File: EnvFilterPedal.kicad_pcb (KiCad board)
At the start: 4 copper layers, 80 x 52 mm, 114 parts, among them J101 ScopeGroundLoop, J102 IO, Q101 BC857, Q102 BC857, Q103 BC847, U101 TL074, U102 TL074, U103 TL074, U104 LM13700, U105 AZ34063U

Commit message: component tweaks after playing thru it for a day
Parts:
- C110: value 10n -> 33n
- R109: value 6k8 -> 5k6
- R111: value 6k8 -> 12k
- R119: value 1k8 -> 2k2
- R136: value 1k8 -> 6k8
- R154: value 4k7 -> 6k8
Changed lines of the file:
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@@
 			)
 		)
-		(property "Value" "10n"
+		(property "Value" "33n"
 			(at 0 -1.679999 90)
 			(layer "B.Fab")
@@
 			)
 		)
-		(property "Value" "1k8"
+		(property "Value" "6k8"
 			(at 0 -1.65 90)
 			(layer "B.Fab")
@@
 			)
 		)
-		(property "Value" "6k8"
+		(property "Value" "12k"
 			(at 0 -1.65 90)
 			(layer "B.Fab")
@@
 			)
 		)
-		(property "Value" "6k8"
+		(property "Value" "5k6"
 			(at 0 -1.65 0)
 			(layer "B.Fab")
@@
 			)
 		)
-		(property "Value" "4k7"
+		(property "Value" "6k8"
 			(at 0 -1.65 0)
 			(layer "B.Fab")
@@
 			)
 		)
-		(property "Value" "1k8"
+		(property "Value" "2k2"
 			(at 0 -1.65 90)
 			(layer "B.Fab")

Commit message: minor value tweaks
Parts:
- R109: value 5k6 -> 5k1
- R111: value 12k -> 10k
- R154: value 6k8 -> 12k
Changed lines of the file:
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@@
 			)
 		)
-		(property "Value" "12k"
+		(property "Value" "10k"
 			(at 0 -1.65 90)
 			(layer "B.Fab")
@@
 			)
 		)
-		(property "Value" "5k6"
+		(property "Value" "5k1"
 			(at 0 -1.65 0)
 			(layer "B.Fab")
@@
 			)
 		)
-		(property "Value" "6k8"
+		(property "Value" "12k"
 			(at 0 -1.65 0)
 			(layer "B.Fab")

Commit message: added SMPS input filtering
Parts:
- added C1: 220u, Capacitor_THT:CP_Radial_D5.0mm_P2.00mm, B.Cu at (69.5, 88.2)
- added FB1: 90R, Inductor_SMD:L_0805_2012Metric, F.Cu at (68.9, 85.5)
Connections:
- C127 pad 1: +9V -> Net-(U105-VCC)
- R148 pad 1: +9V -> Net-(U105-VCC)
- U105 pad 6: +9V -> Net-(U105-VCC)
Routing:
- net Net-(U105-VCC): track 0.00 -> 22.2 mm
- net +9V: track 199.0 -> 182.5 mm
- net GND: vias 106 -> 103

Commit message: rev3 sent to fab
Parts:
- moved FB1 1.10 mm to (70.0, 85.5)
- turned TP101 to 180 degrees
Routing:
- net Net-(R140-Pad2): track 73.1 -> 71.5 mm
- net +9V: track 182.5 -> 183.6 mm
- net GND: vias 103 -> 102
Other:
- board text added: "Rev. 3- Feb 2025 Hayden Setlik"
- board text removed: "Rev. 2- Jan 2025 Hayden Setlik"
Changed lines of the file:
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@@
 	(footprint "Inductor_SMD:L_0805_2012Metric"
 		(layer "F.Cu")
-		(at 68.9 85.5)
+		(at 70 85.5)
 		(descr "Inductor SMD 0805 (2012 Metric), square (rectangular) end terminal, IPC_7351 nominal, (Body size source: IPC-SM-782 page 80, https://www.pcb-3d.com/wordpress/wp-content/uploads/ipc-sm-782a_amendment_1_and_2.pdf), generated with kicad-footprint-generator")
 		(tags "inductor")
@@
 	(footprint "TestPoint:TestPoint_THTPad_D2.0mm_Drill1.0mm_VAL"
 		(layer "B.Cu")
-		(at 39.6 65.275)
+		(at 39.6 65.275 180)
 		(descr "THT pad as test Point, diameter 1.5mm, hole diameter 0.7mm")
 		(tags "test point THT pad")
 		(property "Reference" "TP101"
-			(at 0 1.648 0)
+			(at 0 1.648 360)
 			(layer "B.SilkS")
 			(hide yes)
@@
 		)
 		(property "Value" "In"
-			(at 0 -2.000001 0)
+			(at 0 -2.000001 360)
 			(layer "B.SilkS")
 			(effects
@@
 		)
 		(property "Footprint" "TestPoint:TestPoint_THTPad_D2.0mm_Drill1.0mm_VAL"
-			(at 0 0 180)
+			(at 0 0 0)
 			(unlocked yes)
 			(layer "B.Fab")
@@
 		)
 		(property "Datasheet" ""
-			(at 0 0 180)
+			(at 0 0 0)
 			(unlocked yes)
 			(layer "B.Fab")
@@
 		)
 		(property "Description" "test point"
-			(at 0 0 180)
+			(at 0 0 0)
 			(unlocked yes)
 			(layer "B.Fab")
@@
 		)
 		(fp_text user "${VALUE}"
-			(at 0.01 -2.600001 180)
+			(at 0.01 -2.600001 0)
 			(unlocked yes)
 			(layer "F.SilkS")
@@
 		)
 		(fp_text user "${REFERENCE}"
-			(at 0 1.65 0)
+			(at 0 1.65 360)
 			(layer "B.Fab")
 			(effects
@@
 		)
 		(pad "1" thru_hole circle
-			(at 0 0)
+			(at 0 0 180)
 			(size 2 2)
 			(drill 1)
@@
 		)
 	)
-	(gr_text "Rev. 2- Jan 2025\nHayden Setlik"
+	(gr_text "Rev. 3- Feb 2025\nHayden Setlik"
 		(at 82.75 52.25 0)
 		(layer "B.SilkS")
@@
 	)
 	(via
-		(at 71.05 85.75)
-		(size 0.8)
-		(drill 0.4)
-		(layers "F.Cu" "B.Cu")
-		(free yes)
-		(net 1)
-	)
-	(via
 		(at 78.65 80.05)
 		(size 0.6)
@@
 	)
 	(segment
-		(start 44.95 62.45)
-		(end 44.95 60.65)
+		(start 67.8 85.5)
+		(end 65 88.3)
 		(width 0.35)
 		(layer "F.Cu")
@@
 	)
 	(segment
-		(start 8.1 63.45)
-		(end 14.025 57.525)
+		(start 65 88.3)
+		(end 58.85 88.3)
 		(width 0.35)
 		(layer "F.Cu")
@@
 	)
 	(segment
-		(start 50.25 76.1)
-		(end 50.25 77.5)
+		(start 44.95 62.45)
+		(end 44.95 60.65)
 		(width 0.35)
 		(layer "F.Cu")
@@
 	)
 	(segment
-		(start 67.8 85.5)
-		(end 65 88.3)
+		(start 8.1 63.45)
+		(end 14.025 57.525)
 		(width 0.35)
 		(layer "F.Cu")
@@
 	)
 	(segment
-		(start 67.8375 85.5)
-		(end 67.8 85.5)
+		(start 50.25 76.1)
+		(end 50.25 77.5)
 		(width 0.35)
 		(layer "F.Cu")
@@
 	)
 	(segment
+		(start 55.375 84.825)
+		(end 50.25 84.825)
+		(width 0.35)
+		(layer "F.Cu")
+		(net 3)
+	)
+	(segment
 		(start 8.15 78.75)
 		(end 8.1 78.7)
@@
 	)
 	(segment
-		(start 55.375 84.825)
-		(end 50.25 84.825)
-		(width 0.35)
-		(layer "F.Cu")
-		(net 3)
-	)
-	(segment
 		(start 24.7 46.85)
 		(end 30.715 46.85)
@@
 	)
 	(segment
-		(start 58.85 88.3)
-		(end 55.375 84.825)
+		(start 44.95 62.45)
+		(end 52 62.45)
 		(width 0.35)
 		(layer "F.Cu")
@@
 	)
 	(segment
-		(start 44.95 62.45)
-		(end 52 62.45)
+		(start 52 62.45)
+		(end 55.15 65.6)
 		(width 0.35)
 		(layer "F.Cu")
@@
 	)
 	(segment
-		(start 52 62.45)
-		(end 55.15 65.6)
+		(start 58.85 88.3)
+		(end 55.375 84.825)
 		(width 0.35)
 		(layer "F.Cu")
@@
 	)
 	(segment
-		(start 14.025 57.525)
-		(end 24.7 46.85)
+		(start 68.9375 85.5)
+		(end 67.8 85.5)
 		(width 0.35)
 		(layer "F.Cu")
@@
 	)
 	(segment
-		(start 55.15 65.6)
-		(end 55.15 71.2)
+		(start 14.025 57.525)
+		(end 24.7 46.85)
 		(width 0.35)
 		(layer "F.Cu")
@@
 	)
 	(segment
-		(start 65 88.3)
-		(end 58.85 88.3)
+		(start 55.15 65.6)
+		(end 55.15 71.2)
 		(width 0.35)
 		(layer "F.Cu")
@@
 	(segment
 		(start 64.775 77.700001)
-		(end 57.544999 77.700001)
+		(end 64.525001 77.95)
 		(width 0.18)
 		(layer "B.Cu")
@@
 	)
 	(segment
+		(start 64.525001 77.95)
+		(end 57.295 77.95)
+		(width 0.18)
+		(layer "B.Cu")
+		(net 9)
+	)
+	(segment
 		(start 57.1925 62.3425)
 		(end 52.275 62.3425)
@@
 	)
 	(segment
-		(start 57.544999 77.700001)
+		(start 57.295 77.95)
 		(end 57.275 77.97)
 		(width 0.18)
@@
 	)
 	(segment
-		(start 52.6 85.6)
-		(end 51.15 87.05)
+		(start 67 93)
+		(end 67 90.95)
 		(width 0.18)
 		(layer "B.Cu")
@@
 	)
 	(segment
-		(start 67 93)
-		(end 67 88.3)
+		(start 43.05 84.95)
+		(end 40.25 87.75)
 		(width 0.18)
 		(layer "B.Cu")
@@
 	)
 	(segment
-		(start 13.08 80.7825)
-		(end 11.775 82.0875)
+		(start 61.65 85.6)
+		(end 52.6 85.6)
 		(width 0.18)
 		(layer "B.Cu")
@@
 	)
 	(segment
-		(start 48.4 87.05)
-		(end 46.3 84.95)
+		(start 13.08 80.7825)
+		(end 11.775 82.0875)
 		(width 0.18)
 		(layer "B.Cu")
@@
 	)
 	(segment
-		(start 46.3 84.95)
-		(end 43.05 84.95)
+		(start 52.6 85.6)
+		(end 51.15 87.05)
 		(width 0.18)
 		(layer "B.Cu")
@@
 	)
 	(segment
-		(start 51.15 87.05)
-		(end 48.4 87.05)
+		(start 14.25 80.7825)
+		(end 13.08 80.7825)
 		(width 0.18)
 		(layer "B.Cu")
@@
 	)
 	(segment
-		(start 14.25 80.7825)
-		(end 13.08 80.7825)
+		(start 46.3 84.95)
+		(end 43.05 84.95)
 		(width 0.18)
 		(layer "B.Cu")
@@
 	)
 	(segment
-		(start 64.3 85.6)
-		(end 52.6 85.6)
+		(start 51.15 87.05)
+		(end 48.4 87.05)
 		(width 0.18)
 		(layer "B.Cu")
@@
 	)
 	(segment
-		(start 43.05 84.95)
-		(end 40.25 87.75)
+		(start 48.4 87.05)
+		(end 46.3 84.95)
 		(width 0.18)
 		(layer "B.Cu")
@@
 	)
 	(segment
-		(start 67 88.3)
-		(end 64.3 85.6)
+		(start 67 90.95)
+		(end 61.65 85.6)
 		(width 0.18)
 		(layer "B.Cu")
@@
 	)
 	(segment
+		(start 71.0625 86.4875)
+		(end 71.0625 85.5)
+		(width 0.35)
+		(layer "F.Cu")
+		(net 71)
+	)
+	(segment
 		(start 71.9 90.75)
 		(end 71.9 89.35)
@@
 	)
 	(segment
-		(start 69.55 88.25)
-		(end 69.55 85.9125)
-		(width 0.35)
-		(layer "F.Cu")
-		(net 71)
-	)
-	(segment
 		(start 78.155 92.795001)
 		(end 78.125 92.825001)
@@
 	)
 	(segment
+		(start 69.55 88)
+		(end 71.0625 86.4875)
+		(width 0.35)
+		(layer "F.Cu")
+		(net 71)
+	)
+	(segment
 		(start 71.9 89.35)
 		(end 70.8 88.25)
@@
 	)
 	(segment
-		(start 69.55 85.9125)
-		(end 69.9625 85.5)
+		(start 78.174999 92.875)
+		(end 78.125 92.825001)
 		(width 0.35)
 		(layer "F.Cu")
@@
 	)
 	(segment
-		(start 78.174999 92.875)
-		(end 78.125 92.825001)
+		(start 69.55 88.25)
+		(end 69.55 88)
 		(width 0.35)
 		(layer "F.Cu")

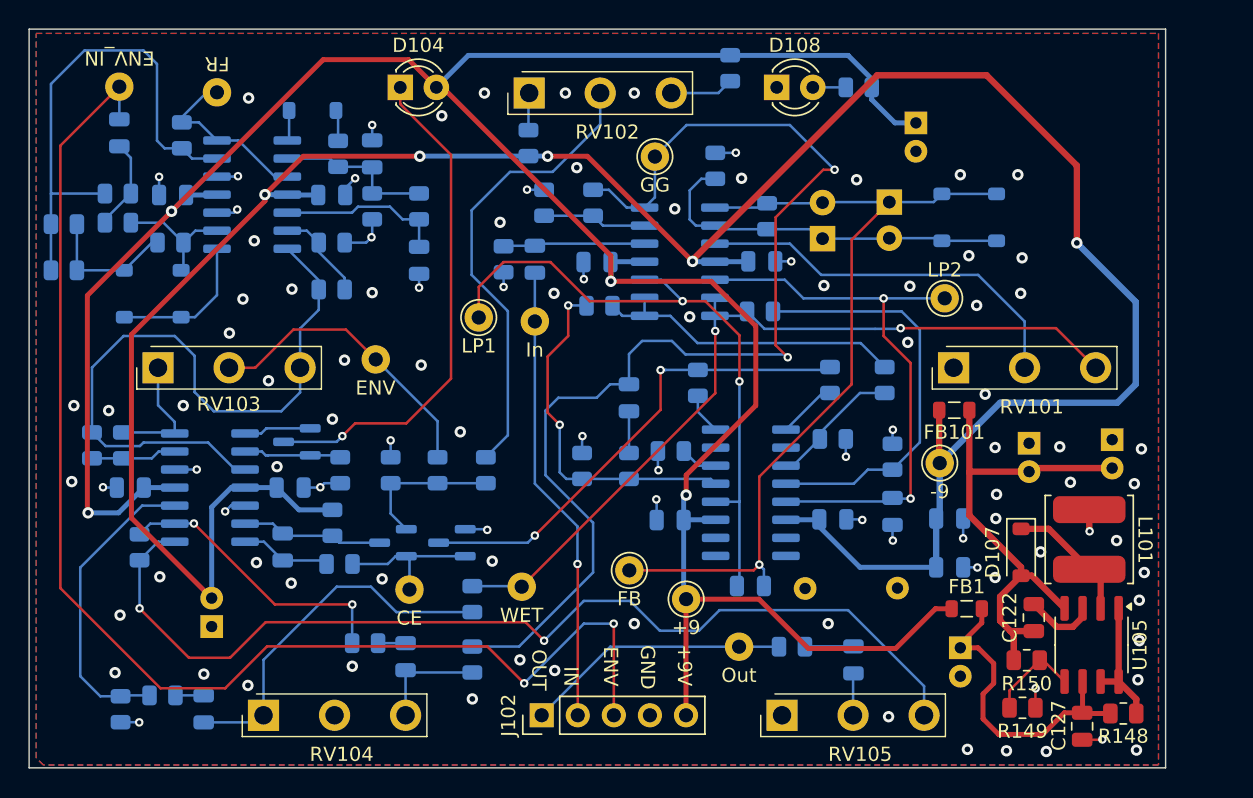
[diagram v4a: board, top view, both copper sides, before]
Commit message: laid out new inductor, some trace cleanup
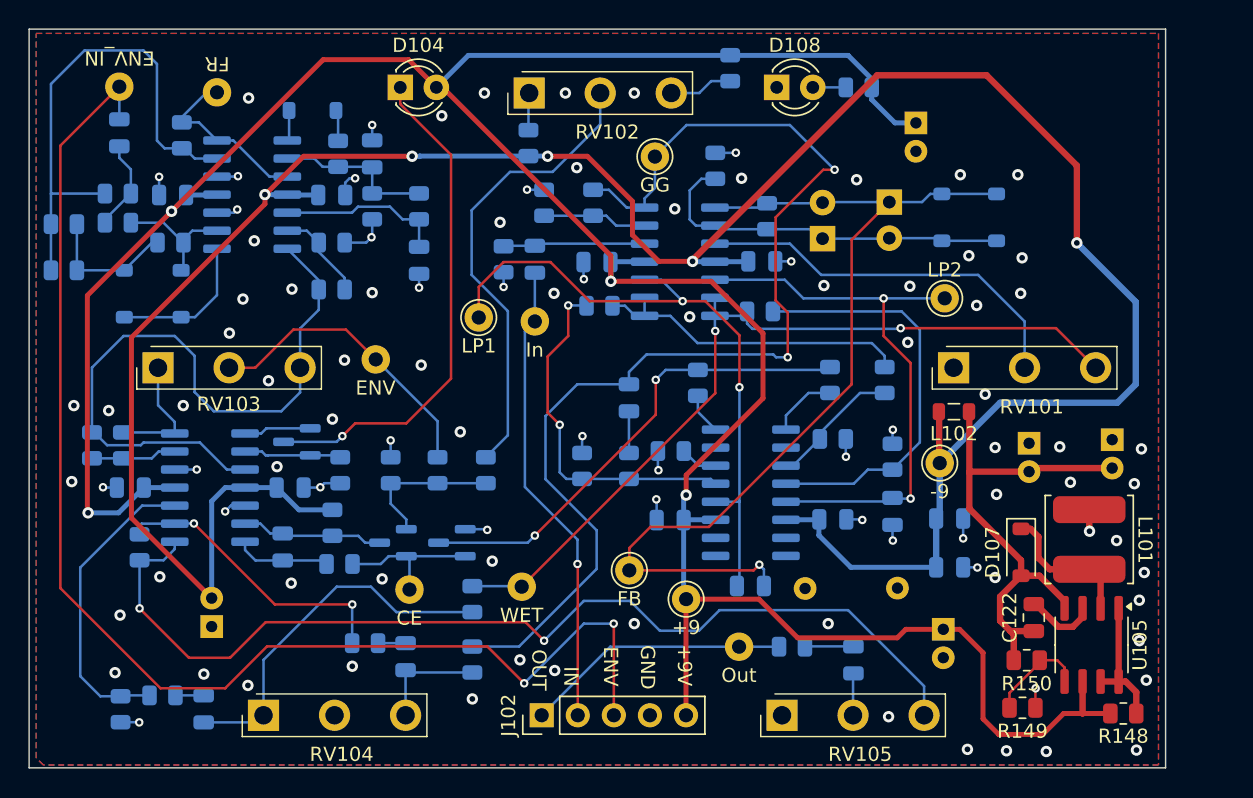
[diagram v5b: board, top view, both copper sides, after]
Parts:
- removed C127: 22u, Capacitor_SMD:C_0805_2012Metric
- removed FB1, FB101: 90R, Inductor_SMD:L_0805_2012Metric
- added L102: 1u, Inductor_SMD:L_0805_2012Metric, F.Cu at (69.1, 71.6)
- C105: value 470u -> 220u
- moved C1 1.77 mm to (68.3, 87.0)
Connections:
- net Net-(D107-A) renamed /-9RAW
- C1 pad 1: Net-(U105-VCC) -> +9V
- R148 pad 1: Net-(U105-VCC) -> +9V
- U105 pad 6: Net-(U105-VCC) -> +9V
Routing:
- net Net-(U105-VCC): track 22.7 -> 0.00 mm
- net +9V: track 183.6 -> 202.6 mm
- net /Feedback: track 60.5 -> 67.1 mm
- net -9V: track 184.9 -> 187.0 mm
- net /GTR_GAIN: track 82.9 -> 81.3 mm
- net GND: track 43.4 -> 42.2 mm, vias 102 -> 98
- net /SWE: track 9.06 -> 9.93 mm
- net Net-(R134-Pad2): track 4.17 -> 4.75 mm
- net Net-(U105-FB): track 6.60 -> 7.18 mm
- net FX_IN: track 32.4 -> 33.0 mm
- net /WET: track 58.1 -> 58.6 mm
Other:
- board text added: "Rev. 4- 03/2026 Hayden Setlik"
- board text removed: "Rev. 3- Feb 2025 Hayden Setlik"

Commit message: new layout
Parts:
- removed C101, C102, C103, C106, C108, C111, C112, C114, C115, C126: 100n, Capacitor_SMD:C_0805_2012Metric
- removed C104, C109, C113, C118, C119, C120, C125: 1u, Capacitor_SMD:C_0805_2012Metric
- removed C105: 220u, Capacitor_THT:CP_Radial_D5.0mm_P2.00mm
- removed C107: 4n7, Capacitor_SMD:C_0805_2012Metric
- removed C110: 33n, Capacitor_SMD:C_0805_2012Metric
- removed C116, C117: 1n, Capacitor_SMD:C_0805_2012Metric
- removed C121: 100u, Capacitor_THT:CP_Radial_D5.0mm_P2.00mm
- removed C122: 470p, Capacitor_SMD:C_0805_2012Metric
- removed C123, C124: 470u, Capacitor_THT:CP_Radial_D5.0mm_P2.00mm
- removed D101, D102, D103, D109, D110: 1N4148W, Diode_SMD:D_SOD-123
- removed D104, D105, D106, D108: LED, LED_THT:LED_D3.0mm
- removed D107: PMEG3030, Diode_SMD:D_SOD-123
- removed J101: ScopeGroundLoop, Connector:THT_GND_WIRE
- removed J102: IO, Connector_PinHeader_2.54mm:PinHeader_1x05_P2.54mm_Vertical
- removed L101: 68uH, Inductor_SMD:L_TDK_VLS6045EX_VLS6045AF
- removed L102: 1u, Inductor_SMD:L_0805_2012Metric
- removed Q101, Q102: BC857, Package_TO_SOT_SMD:SOT-23
- removed Q103: BC847, Package_TO_SOT_SMD:SOT-23
- removed R101, R102, R103, R104, R105, R108, R112, R113, R117, R118, R120, R124: 100k, Resistor_SMD:R_0805_2012Metric
- removed R106, R125, R126, R129, R130: 1k, Resistor_SMD:R_0805_2012Metric
- removed R107: 22k, Resistor_SMD:R_0805_2012Metric
- removed R109: 5k1, Resistor_SMD:R_0805_2012Metric
- removed R110, R136: 6k8, Resistor_SMD:R_0805_2012Metric
- removed R111, R135: 10k, Resistor_SMD:R_0805_2012Metric
- removed R114, R119: 2k2, Resistor_SMD:R_0805_2012Metric
- removed R115, R137, R139: 470k, Resistor_SMD:R_0805_2012Metric
- removed R116, R133, R134: 4k7, Resistor_SMD:R_0805_2012Metric
- removed R121: 1M, Resistor_SMD:R_0805_2012Metric
- removed R122, R141, R142: 47k, Resistor_SMD:R_0805_2012Metric
- removed R123, R154: 12k, Resistor_SMD:R_0805_2012Metric
- removed R127, R128, R131, R132: 33k, Resistor_SMD:R_0805_2012Metric
- removed R138, R140: 1Meg, Resistor_SMD:R_0805_2012Metric
- removed R143: 220, Resistor_SMD:R_0805_2012Metric
- removed R148: 0.24R, Resistor_SMD:R_0805_2012Metric
- removed R149: 51k, Resistor_SMD:R_0805_2012Metric
- removed R150: 8k2, Resistor_SMD:R_0805_2012Metric
- removed RV101, RV104: 100kB, Potentiometer_THT:Potentiometer_Alpha_RV16AF_42_VeryLong
- removed RV102, RV103: 10kB, Potentiometer_THT:Potentiometer_Alpha_RV16AF_42_VeryLong
- removed RV105: 100kA, Potentiometer_THT:Potentiometer_Alpha_RV16AF_42_VeryLong
- removed TP101: In, TestPoint:TestPoint_THTPad_D2.0mm_Drill1.0mm_VAL
- removed TP102: Out, TestPoint:TestPoint_THTPad_D2.0mm_Drill1.0mm_VAL
- removed TP103: CE, TestPoint:TestPoint_THTPad_D2.0mm_Drill1.0mm_VAL
- removed TP104: WET, TestPoint:TestPoint_THTPad_D2.0mm_Drill1.0mm_VAL
- removed TP105: ENV, TestPoint:TestPoint_THTPad_D2.0mm_Drill1.0mm_VAL
- removed TP106: ENV_IN, TestPoint:TestPoint_THTPad_D2.0mm_Drill1.0mm_VAL
- removed TP107: GG, TestPoint:TestPoint_THTPad_D2.0mm_Drill1.0mm_VAL
- removed TP108: FR, TestPoint:TestPoint_THTPad_D2.0mm_Drill1.0mm_VAL
- removed TP109: +9, TestPoint:TestPoint_THTPad_D2.0mm_Drill1.0mm_VAL
- removed TP110: -9, TestPoint:TestPoint_THTPad_D2.0mm_Drill1.0mm_VAL
- removed TP111: LP1, TestPoint:TestPoint_THTPad_D2.0mm_Drill1.0mm_VAL
- removed TP112: LP2, TestPoint:TestPoint_THTPad_D2.0mm_Drill1.0mm_VAL
- removed TP113: FB, TestPoint:TestPoint_THTPad_D2.0mm_Drill1.0mm_VAL
- removed U101, U102, U103: TL074, Package_SO:SOIC-14_3.9x8.7mm_P1.27mm
- removed U104: LM13700, Package_SO:SOIC-16_3.9x9.9mm_P1.27mm
- removed U105: AZ34063U, Package_SO:SO-8_3.9x4.9mm_P1.27mm
- added C10: 100n, Capacitor_SMD:C_0805_2012Metric, B.Cu at (60.4, 80.2)
- added C11: 1u, Capacitor_SMD:C_0805_2012Metric, B.Cu at (15.0, 60.9)
- added C12: 1u, Capacitor_SMD:C_0805_2012Metric, B.Cu at (44.9, 69.8)
- added C13: 33n, Capacitor_SMD:C_0805_2012Metric, B.Cu at (11.5, 53.6)
- added C14: 1n, Capacitor_SMD:C_0805_2012Metric, B.Cu at (59.3, 54.0)
- added C15: 1n, Capacitor_SMD:C_0805_2012Metric, B.Cu at (63.9, 80.1)
- added C16: 4n7, Capacitor_SMD:C_0805_2012Metric, B.Cu at (33.0, 82.9)
- added C17: 220u, Capacitor_THT:CP_Radial_D5.0mm_P2.00mm, B.Cu at (78.1, 74.3)
- added C18: 1u, Capacitor_SMD:C_0805_2012Metric, B.Cu at (16.3, 83.7)
- added C19: 1u, Capacitor_SMD:C_0805_2012Metric, B.Cu at (11.8, 79.8)
- added C2: 100n, Capacitor_SMD:C_0805_2012Metric, B.Cu at (17.6, 57.7)
- added C20: 470p, Capacitor_SMD:C_0805_2012Metric, F.Cu at (79.3, 85.2)
- added C21: 220u, Capacitor_THT:CP_Radial_D5.0mm_P2.00mm, B.Cu at (85.1, 85.1)
- added C22: 470u, Capacitor_THT:CP_Radial_D5.0mm_P2.00mm, B.Cu at (85.0, 78.3)
- added C23: 1u, Capacitor_SMD:C_0805_2012Metric, B.Cu at (62.1, 88.6)
- added C24: 220u, Capacitor_THT:CP_Radial_D5.0mm_P2.00mm, B.Cu at (79.0, 91.4)
- added C25: 100u, Capacitor_THT:CP_Radial_D5.0mm_P2.00mm, B.Cu at (70.5, 74.2)
- added C26: 10u, Capacitor_SMD:C_0805_2012Metric, F.Cu at (76.8, 92.8)
- added C3: 100n, Capacitor_SMD:C_0805_2012Metric, B.Cu at (22.6, 79.4)
- added C4: 100n, Capacitor_SMD:C_0805_2012Metric, B.Cu at (33.7, 79.4)
- added C5: 100n, Capacitor_SMD:C_0805_2012Metric, B.Cu at (35.3, 59.4)
- added C6: 1u, Capacitor_SMD:C_0805_2012Metric, B.Cu at (47.0, 60.4)
- added C7: 100n, Capacitor_SMD:C_0805_2012Metric, B.Cu at (53.5, 61.0)
- added C8: 100n, Capacitor_SMD:C_0805_2012Metric, B.Cu at (64.8, 61.0)
- added C9: 100n, Capacitor_SMD:C_0805_2012Metric, B.Cu at (49.2, 80.2)
- added D1: 1N4148W, Diode_SMD:D_SOD-123, B.Cu at (29.4, 54.9)
- added D2: 1N4148W, Diode_SMD:D_SOD-123, B.Cu at (20.9, 50.0)
- added D3: 1N4148W, Diode_SMD:D_SOD-123, B.Cu at (20.8, 63.7)
- added D4: 1N4148W, Diode_SMD:D_SOD-123, B.Cu at (68.4, 56.1)
- added D5: 1N4148W, Diode_SMD:D_SOD-123, B.Cu at (72.1, 56.1)
- added D6: LED, LED_THT:LED_D3.0mm, B.Cu at (33.0, 48.8)
- added D7: PMEG3030, Diode_SMD:D_SOD-123, F.Cu at (80.0, 88.6)
- added D8: LED, LED_THT:LED_D3.0mm, B.Cu at (56.0, 48.8)
- added J1: ScopeGroundLoop, Connector_Pin:THT_GND_WIRE, B.Cu at (10.9, 90.6)
- added J2: IO, Connector_PinHeader_2.54mm:PinHeader_1x05_P2.54mm_Vertical, F.Cu at (39.9, 93.2)
- added L1: 68uH, Inductor_SMD:L_TDK_VLS6045EX_VLS6045AF, F.Cu at (74.0, 86.8)
- added L2: 4u7, Inductor_SMD:L_Bourns_SRP3212, F.Cu at (82.3, 92.4)
- added Q1: BC847, Package_TO_SOT_SMD:SOT-23, B.Cu at (34.0, 73.5)
- added Q2: BC857, Package_TO_SOT_SMD:SOT-23, B.Cu at (37.5, 81.5)
- added Q3: BC857, Package_TO_SOT_SMD:SOT-23, B.Cu at (41.7, 81.5)
- added R1: 100k, Resistor_SMD:R_0805_2012Metric, B.Cu at (36.2, 55.9)
- added R10: 47k, Resistor_SMD:R_0805_2012Metric, B.Cu at (34.2, 55.9)
- added R11: 100k, Resistor_SMD:R_0805_2012Metric, B.Cu at (31.9, 59.4)
- added R12: 22k, Resistor_SMD:R_0805_2012Metric, B.Cu at (14.8, 57.3)
- added R13: 33k, Resistor_SMD:R_0805_2012Metric, B.Cu at (44.9, 73.6)
- added R14: 100k, Resistor_SMD:R_0805_2012Metric, B.Cu at (28.8, 61.6)
- added R15: 1k, Resistor_SMD:R_0805_2012Metric, B.Cu at (48.0, 76.9)
- added R16: 100k, Resistor_SMD:R_0805_2012Metric, B.Cu at (11.5, 57.3)
- added R17: 1k, Resistor_SMD:R_0805_2012Metric, B.Cu at (48.1, 73.7)
- added R18: 33k, Resistor_SMD:R_0805_2012Metric, B.Cu at (53.4, 64.9)
- added R19: 4k7, Resistor_SMD:R_0805_2012Metric, B.Cu at (52.3, 70.0)
- added R2: 1M, Resistor_SMD:R_0805_2012Metric, B.Cu at (50.5, 60.4)
- added R20: 5k1, Resistor_SMD:R_0805_2012Metric, B.Cu at (13.9, 53.6)
- added R21: 100k, Resistor_SMD:R_0805_2012Metric, B.Cu at (17.1, 53.6)
- added R22: 10k, Resistor_SMD:R_0805_2012Metric, B.Cu at (65.4, 56.9)
- added R23: 33k, Resistor_SMD:R_0805_2012Metric, B.Cu at (61.1, 70.0)
- added R24: 1k, Resistor_SMD:R_0805_2012Metric, B.Cu at (62.0, 77.4)
- added R25: 2k2, Resistor_SMD:R_0805_2012Metric, B.Cu at (30.1, 73.6)
- added R26: 6k8, Resistor_SMD:R_0805_2012Metric, B.Cu at (68.4, 60.3)
- added R27: 1k, Resistor_SMD:R_0805_2012Metric, B.Cu at (62.0, 74.1)
- added R28: 33k, Resistor_SMD:R_0805_2012Metric, B.Cu at (64.3, 70.0)
- added R29: 4k7, Resistor_SMD:R_0805_2012Metric, B.Cu at (57.2, 70.0)
- added R3: 100k, Resistor_SMD:R_0805_2012Metric, B.Cu at (28.1, 68.8)
- added R30: 6k8, Resistor_SMD:R_0805_2012Metric, B.Cu at (49.2, 52.3)
- added R31: 10k, Resistor_SMD:R_0805_2012Metric, B.Cu at (39.2, 52.3)
- added R32: 100k, Resistor_SMD:R_0805_2012Metric, B.Cu at (18.1, 71.8)
- added R33: 100k, Resistor_SMD:R_0805_2012Metric, B.Cu at (44.2, 52.6)
- added R34: 2k2, Resistor_SMD:R_0805_2012Metric, B.Cu at (39.9, 76.6)
- added R35: 470k, Resistor_SMD:R_0805_2012Metric, B.Cu at (36.6, 76.6)
- added R36: 4k7, Resistor_SMD:R_0805_2012Metric, B.Cu at (34.0, 85.7)
- added R37: 0.24R, Resistor_SMD:R_0805_2012Metric, F.Cu at (75.4, 73.6)
- added R38: 47k, Resistor_SMD:R_0805_2012Metric, B.Cu at (21.1, 88.8)
- added R39: 47k, Resistor_SMD:R_0805_2012Metric, B.Cu at (31.1, 88.8)
- added R4: 12k, Resistor_SMD:R_0805_2012Metric, B.Cu at (49.6, 56.5)
- added R40: 51k, Resistor_SMD:R_0805_2012Metric, F.Cu at (80.3, 78.7)
- added R41: 8k2, Resistor_SMD:R_0805_2012Metric, F.Cu at (80.3, 82.3)
- added R42: 470k, Resistor_SMD:R_0805_2012Metric, B.Cu at (19.7, 83.7)
- added R43: 470k, Resistor_SMD:R_0805_2012Metric, B.Cu at (15.2, 79.8)
- added R44: 1Meg, Resistor_SMD:R_0805_2012Metric, B.Cu at (18.4, 79.8)
- added R45: 1Meg, Resistor_SMD:R_0805_2012Metric, B.Cu at (23.0, 83.7)
- added R46: 220, Resistor_SMD:R_0805_2012Metric, B.Cu at (58.0, 88.6)
- added R47: 12k, Resistor_SMD:R_0805_2012Metric, B.Cu at (63.1, 49.4)
- added R5: 100k, Resistor_SMD:R_0805_2012Metric, B.Cu at (26.2, 51.0)
- added R6: 47k, Resistor_SMD:R_0805_2012Metric, B.Cu at (52.9, 56.5)
- added R7: 100k, Resistor_SMD:R_0805_2012Metric, B.Cu at (22.5, 75.6)
- added R8: 1k, Resistor_SMD:R_0805_2012Metric, B.Cu at (17.1, 60.9)
- added RV1: 10kB, Potentiometer_THT:Potentiometer_Alpha_RV16AF_42_Single_Long, F.Cu at (13.1, 68.5)
- added RV2: 10kB, Potentiometer_THT:Potentiometer_Alpha_RV16AF_42_Single_Long, F.Cu at (39.2, 49.2)
- added RV3: 100kB, Potentiometer_THT:Potentiometer_Alpha_RV16AF_42_Single_Long, F.Cu at (69.1, 68.5)
- added RV4: 100kB, Potentiometer_THT:Potentiometer_Alpha_RV16AF_42_Single_Long, F.Cu at (20.5, 93.0)
- added RV5: 100kA, Potentiometer_THT:Potentiometer_Alpha_RV16AF_42_Single_Long, F.Cu at (57.0, 93.0)
- added TP1: LP1, TestPoint:TestPoint_THTPad_D2.0mm_Drill1.0mm_VAL, B.Cu at (49.5, 63.6)
- added TP10: ENV, TestPoint:TestPoint_THTPad_D2.0mm_Drill1.0mm_VAL, B.Cu at (16.1, 65.6)
- added TP11: ENV_IN, TestPoint:TestPoint_THTPad_D2.0mm_Drill1.0mm_VAL, B.Cu at (35.3, 62.7)
- added TP12: +9, TestPoint:TestPoint_THTPad_D2.0mm_Drill1.0mm_VAL, B.Cu at (50.1, 84.4)
- added TP13: -9, TestPoint:TestPoint_THTPad_D2.0mm_Drill1.0mm_VAL, F.Cu at (73.0, 93.1)
- added TP14: -9R, TestPoint:TestPoint_THTPad_D2.0mm_Drill1.0mm_VAL, F.Cu at (85.7, 89.0)
- added TP2: In, TestPoint:TestPoint_THTPad_D2.0mm_Drill1.0mm_VAL, B.Cu at (43.3, 59.6)
- added TP3: LP2, TestPoint:TestPoint_THTPad_D2.0mm_Drill1.0mm_VAL, B.Cu at (65.8, 63.8)
- added TP4: Out, TestPoint:TestPoint_THTPad_D2.0mm_Drill1.0mm_VAL, B.Cu at (54.8, 88.5)
- added TP5: FR, TestPoint:TestPoint_THTPad_D2.0mm_Drill1.0mm_VAL, B.Cu at (27.9, 65.2)
- added TP6: GG, TestPoint:TestPoint_THTPad_D2.0mm_Drill1.0mm_VAL, B.Cu at (45.0, 65.4)
- added TP7: FB, TestPoint:TestPoint_THTPad_D2.0mm_Drill1.0mm_VAL, B.Cu at (62.6, 54.0)
- added TP8: CE, TestPoint:TestPoint_THTPad_D2.0mm_Drill1.0mm_VAL, B.Cu at (38.5, 86.0)
- added TP9: WET, TestPoint:TestPoint_THTPad_D2.0mm_Drill1.0mm_VAL, B.Cu at (83.8, 64.8)
- added U1: TL074, Package_SO:SOIC-14_3.9x8.7mm_P1.27mm, B.Cu at (23.1, 57.7)
- added U2: TL074, Package_SO:SOIC-14_3.9x8.7mm_P1.27mm, B.Cu at (28.1, 79.4)
- added U3: TL074, Package_SO:SOIC-14_3.9x8.7mm_P1.27mm, B.Cu at (59.2, 61.0)
- added U4: LM13700, Package_SO:SOIC-16_3.9x9.9mm_P1.27mm, B.Cu at (54.8, 78.3)
- added U5: AZ34063U, Package_SO:SO-8_3.9x4.9mm_P1.27mm, F.Cu at (76.4, 79.6)
- C1: value 220u -> 100n; footprint Capacitor_THT:CP_Radial_D5.0mm_P2.00mm -> Capacitor_SMD:C_0805_2012Metric
- moved C1 49.4 mm to (28.6, 57.7), turned to 0 degrees
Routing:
- net +9V: track 202.6 -> 0.00 mm, vias 4 -> 0
- net -9V: track 187.0 -> 0.00 mm, vias 5 -> 0
- net ENV_IN: track 91.7 -> 0.00 mm, vias 2 -> 0
- net /GTR_GAIN: track 81.3 -> 0.00 mm, vias 2 -> 0
- net Net-(R140-Pad2): track 71.8 -> 0.00 mm, vias 2 -> 0
- net /Feedback: track 67.1 -> 0.00 mm, vias 1 -> 0
- net /WET: track 58.6 -> 0.00 mm, vias 2 -> 0
- net /EnvPos: track 47.3 -> 0.00 mm
- net /LP1: track 46.1 -> 0.00 mm, vias 2 -> 0
- net GND: track 42.2 -> 0.00 mm, vias 98 -> 0
- net /LP2: track 40.5 -> 0.00 mm, vias 2 -> 0
- net /-9RAW: track 36.3 -> 0.00 mm
- net Net-(U101B--): track 35.9 -> 0.00 mm
- net Net-(D104-K): track 35.6 -> 0.00 mm, vias 1 -> 0
- net Iabc: track 34.1 -> 0.00 mm, vias 2 -> 0
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
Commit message: routed, DRC passing
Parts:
- moved R26 3.75 mm to (72.1, 60.3)
- moved TP11 2.20 mm to (37.0, 64.1)
- moved TP13 2.15 mm to (70.9, 93.1)
- moved R3 1.65 mm to (26.4, 68.8)
- moved C26 1.30 mm to (75.5, 92.9)
- moved C24 1.14 mm to (78.8, 92.6)
- moved R25 1.08 mm to (30.1, 72.5)
- moved C22 0.90 mm to (85.9, 78.3)
- moved R10 0.55 mm to (34.7, 55.9)
- moved D1 0.55 mm to (29.9, 54.9)
- moved R1 0.55 mm to (36.8, 55.9)
- moved C13 0.52 mm to (11.5, 53.1)
- moved R20 0.52 mm to (13.9, 53.1)
- moved R21 0.52 mm to (17.1, 53.1)
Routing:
- net -9V: track 0.00 -> 234.9 mm, vias 0 -> 6
- net +9V: track 0.00 -> 214.5 mm, vias 0 -> 4
- net /WET: track 0.00 -> 92.2 mm, vias 0 -> 4
- net /vBase: track 0.00 -> 63.3 mm, vias 0 -> 2
- net /GTR_GAIN: track 0.00 -> 63.1 mm, vias 0 -> 2
- net Net-(R45-Pad2): track 0.00 -> 52.6 mm
- net ENV_IN: track 0.00 -> 49.4 mm
- net /EnvPos: track 0.00 -> 48.5 mm, vias 0 -> 1
- net FX_IN: track 0.00 -> 41.8 mm
- net /LP1: track 0.00 -> 35.2 mm, vias 0 -> 1
- net /LP2: track 0.00 -> 28.3 mm, vias 0 -> 1
- net /-9RAW: track 0.00 -> 28.2 mm
- net Net-(U4A--): track 0.00 -> 28.2 mm, vias 0 -> 2
- net Iabc: track 0.00 -> 27.0 mm, vias 0 -> 2
- net Net-(C18-Pad1): track 0.00 -> 25.7 mm
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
